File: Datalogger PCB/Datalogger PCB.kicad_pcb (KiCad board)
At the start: 2 copper layers, 42.2 x 101.8 mm, 46 parts, among them J1 Conn_01x02_Pin, M1 Motor_Servo, M2 Motor_Servo, M3 Motor_Servo, M4 Motor_Servo, U1 Teensy4.1, U2 BNO055, U3 LPS25HB, U4 AMS1117-5.0, U5 NRF24L01_Breakout, U6 VN5E160STR-E, U7 VN5E160STR-E, U8 VN5E160STR-E, U9 VN5E160STR-E

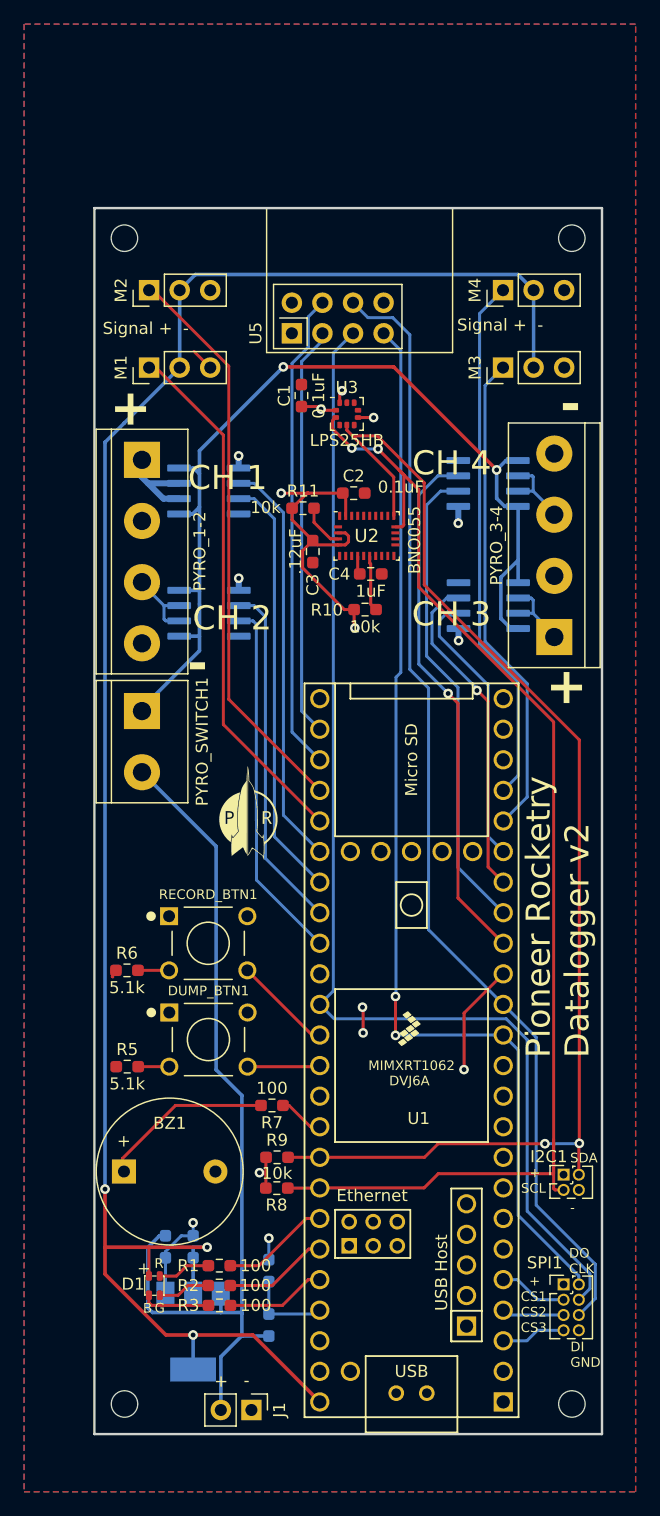
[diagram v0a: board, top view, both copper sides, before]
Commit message: Added serial connector and power connectors
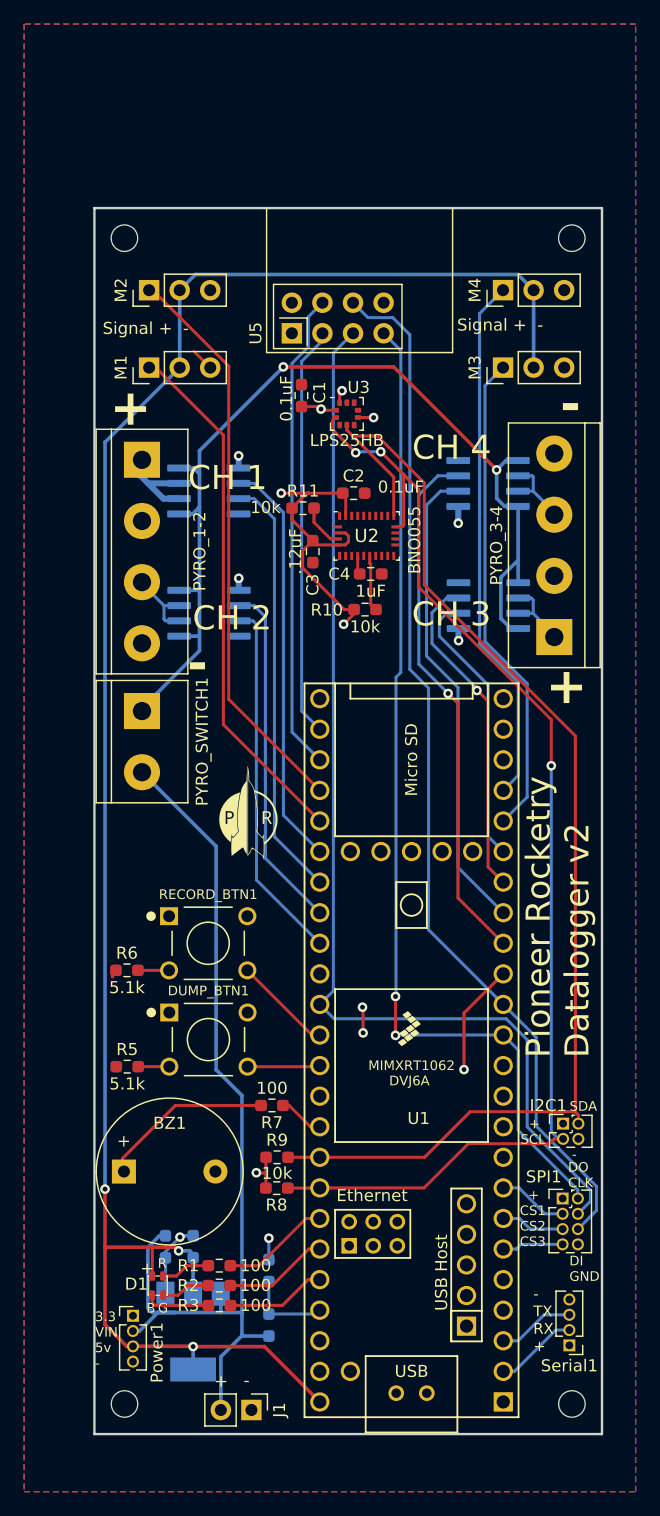
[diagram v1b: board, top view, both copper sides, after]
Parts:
- added Power1: Conn_01x04_Pin, Connector_PinHeader_1.27mm:PinHeader_1x04_P1.27mm_Vertical, F.Cu at (140.8, 134.2)
- added Serial1: Conn_01x04_Pin, Connector_PinHeader_1.27mm:PinHeader_1x04_P1.27mm_Vertical, F.Cu at (177.0, 136.7)
- moved SPI1 7.14 mm to (176.4, 124.5)
- moved I2C1 4.24 mm to (176.5, 118.2)
- moved D1 0.27 mm to (143.2, 132.5)
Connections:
- U1 pad 2: unconnected-(U1-0_RX1_CRX2_CS1-Pad2) -> /RX
- U1 pad 3: /EXTERNAL_CS3 -> /TX
- U1 pad 4: /EXTERNAL_CS2 -> unconnected-(U1-2_OUT2-Pad4)
- U1 pad 5: /EXTERNAL_CS1 -> unconnected-(U1-3_LRCLK2-Pad5)
- U1 pad 6: unconnected-(U1-4_BCLK2-Pad6) -> /EXTERNAL_CS3
- U1 pad 7: unconnected-(U1-5_IN2-Pad7) -> /EXTERNAL_CS2
- U1 pad 8: unconnected-(U1-6_OUT1D-Pad8) -> /EXTERNAL_CS1
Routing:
- net /DO: track 91.4 -> 84.2 mm
- net /CLK: track 99.5 -> 92.4 mm
- net /DI: track 94.2 -> 87.2 mm
- net /RX: track 0.00 -> 6.91 mm
- net /TX: track 0.00 -> 6.38 mm
- net /SCL: track 104.7 -> 99.6 mm, vias 2 -> 3
- net /VIN: track 76.4 -> 80.5 mm
- net /SDA: track 104.2 -> 100.7 mm, vias 2 -> 0
- net +5V: track 162.0 -> 160.8 mm
- net unconnected-(U1-2_OUT2-Pad4): track 0.00 -> 0.57 mm
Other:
- board text added: "- TX RX +"
- board text added: "3.3 VIN 5v -"

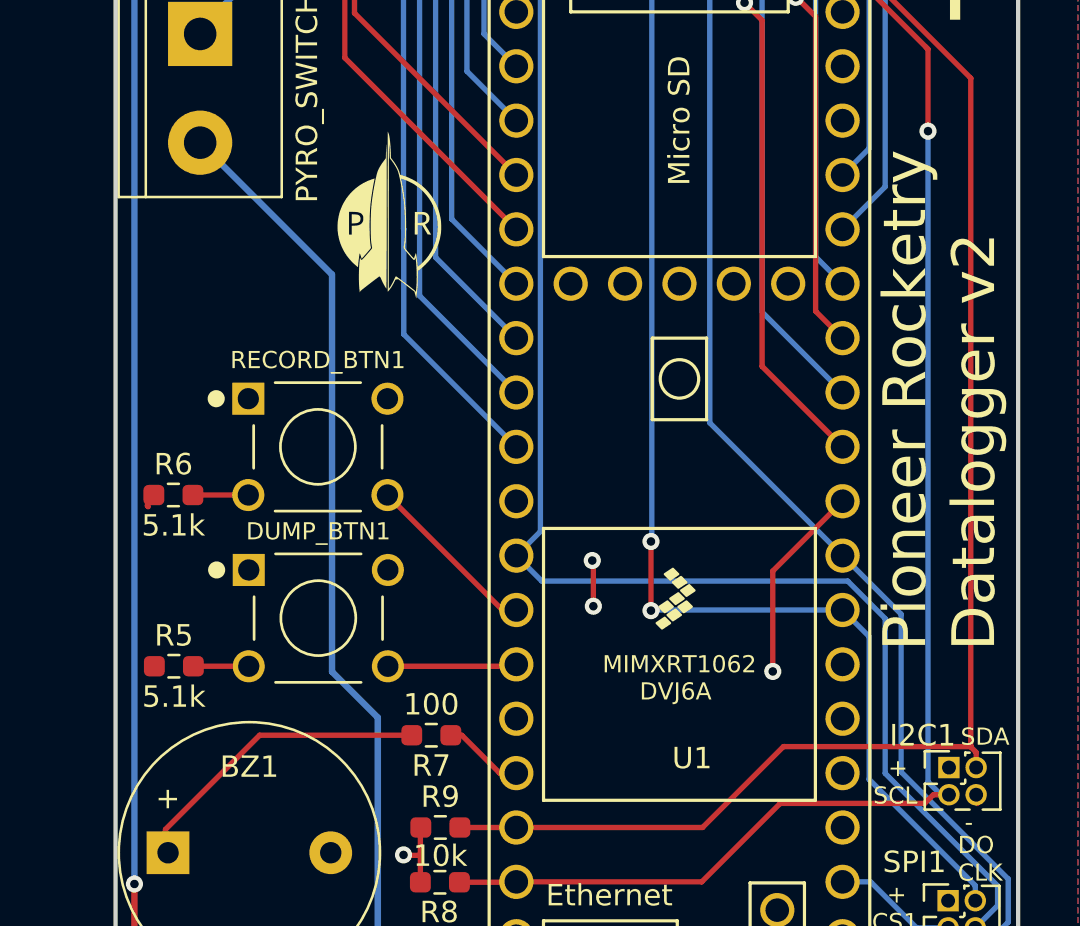
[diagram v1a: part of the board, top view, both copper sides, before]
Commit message: Remove DUMP_BTN
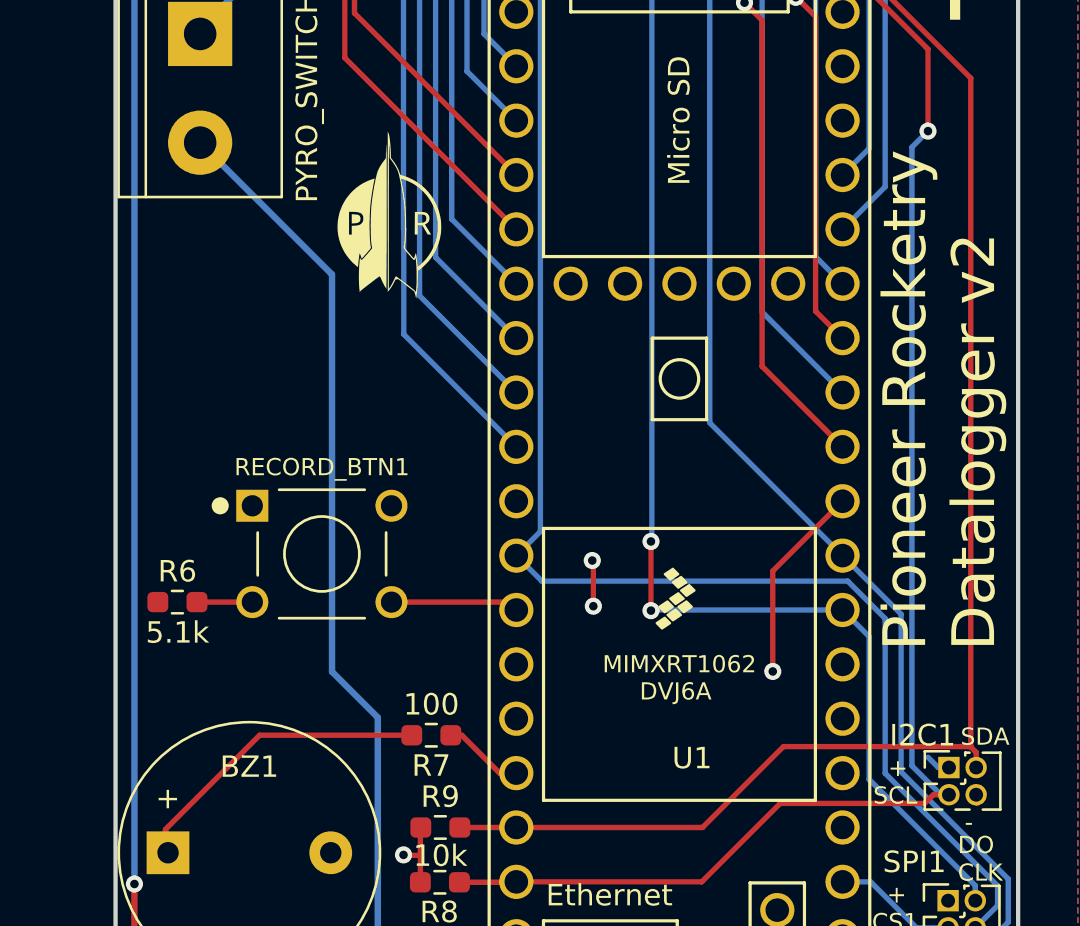
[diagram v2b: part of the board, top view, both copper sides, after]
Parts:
- removed DUMP_BTN1: FSM8JH, Push Button:SW_FSM8JH
- removed R5: 5.1k, Resistor_SMD:R_0603_1608Metric_Pad0.98x0.95mm_HandSolder
- moved R6 5.01 mm to (140.4, 110.5)
- moved RECORD_BTN1 5.01 mm to (147.2, 108.3)
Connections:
- U1 pad 37: /DUMP_BTN -> unconnected-(U1-15_A1_RX3_SPDIF_IN-Pad37)
- U1 pad 38: /ERASE_BTN -> unconnected-(U1-16_A2_RX4_SCL1-Pad38)
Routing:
- net /DUMP_BTN: track 6.04 -> 0.00 mm
- net Net-(DUMP_BTN1-Pad2): track 2.58 -> 0.00 mm
- net /RECORD_BTN: track 8.24 -> 6.63 mm
- net +3.3V: track 47.6 -> 48.8 mm
- net /SCL: track 99.6 -> 100.2 mm

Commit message: Final Revision
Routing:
- net +5V: track 160.8 -> 153.4 mm, vias 3 -> 0
- net /VIN: track 80.5 -> 74.7 mm, vias 0 -> 2
- net /PYRO_POWER: track 82.6 -> 87.4 mm, vias 2 -> 8
- added copper zone on In2.Cu, net +3.3V
- added copper zone on In1.Cu, net GND
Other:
- copper layers 2 -> 4

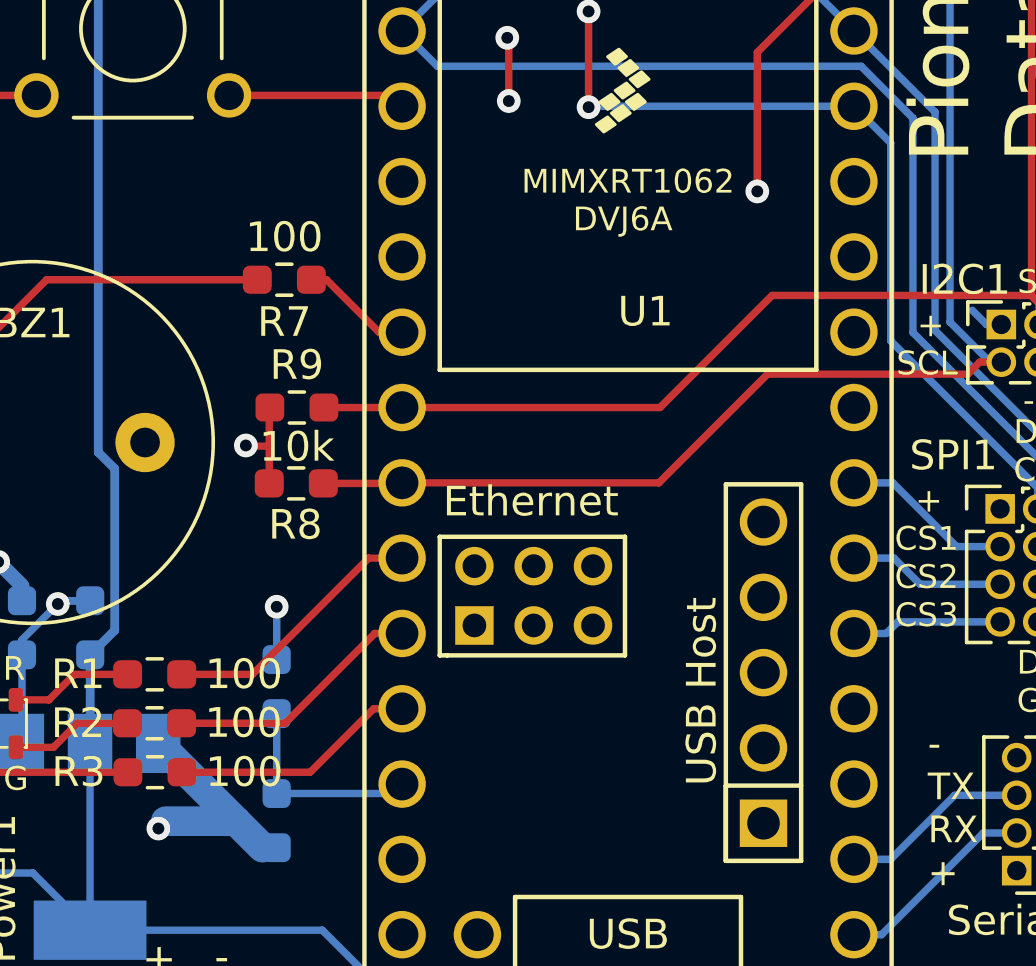
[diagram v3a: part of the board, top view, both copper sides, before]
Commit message: Made LED's connected to PWM pins
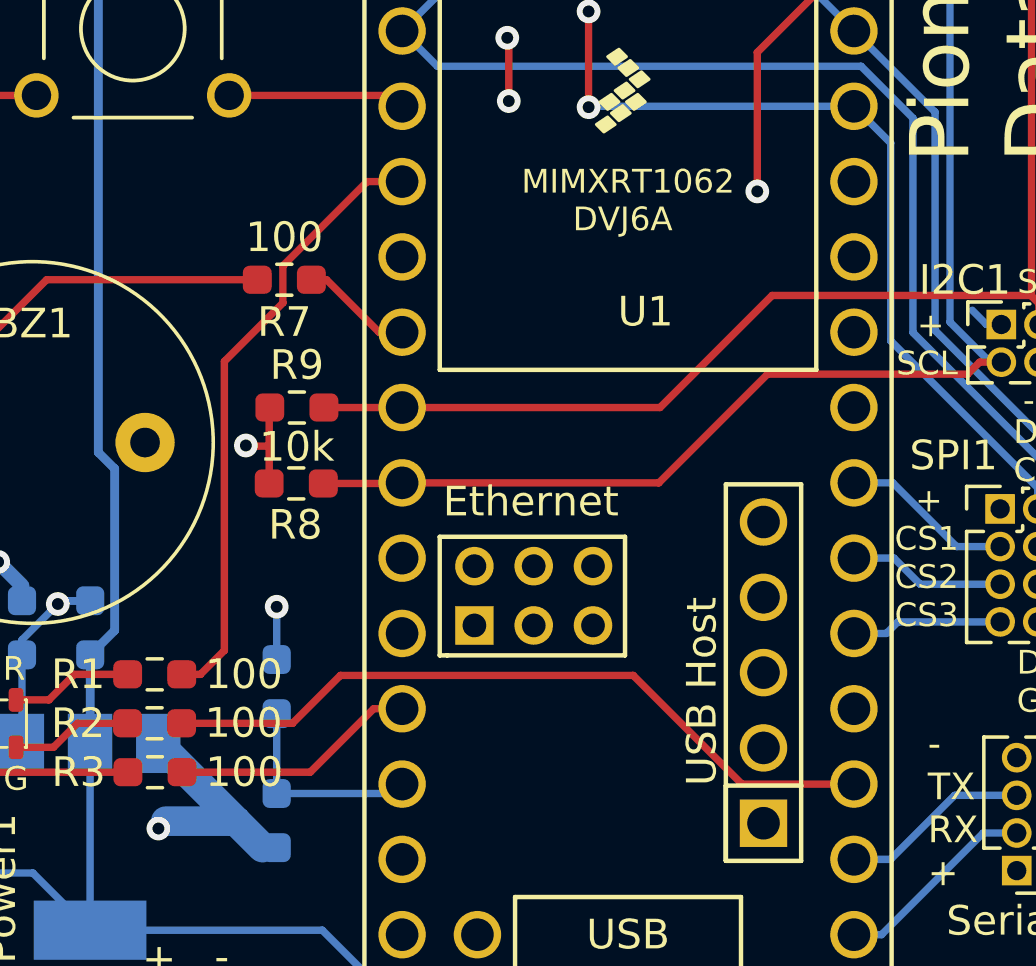
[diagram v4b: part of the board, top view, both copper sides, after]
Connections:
- U1 pad 37: unconnected-(U1-15_A1_RX3_SPDIF_IN-Pad37) -> /RGB-R
- U1 pad 4: unconnected-(U1-2_OUT2-Pad4) -> /RGB-G
- U1 pad 42: /RGB-R -> unconnected-(U1-20_A6_TX5_LRCLK1-Pad42)
- U1 pad 43: /RGB-G -> unconnected-(U1-21_A7_RX5_BCLK1-Pad43)
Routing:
- net /RGB-G: track 8.69 -> 25.4 mm
- net /RGB-R: track 9.06 -> 20.9 mm
- net unconnected-(U1-2_OUT2-Pad4): track 0.57 -> 0.00 mm
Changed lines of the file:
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@@
   (net 1 "GND")
   (net 2 "Net-(BZ1--)")
-  (net 3 "unconnected-(U1-15_A1_RX3_SPDIF_IN-Pad37)")
+  (net 3 "unconnected-(U1-20_A6_TX5_LRCLK1-Pad42)")
   (net 4 "unconnected-(U1-16_A2_RX4_SCL1-Pad38)")
   (net 5 "unconnected-(RECORD_BTN1-Pad3)")
@@
   (net 40 "/TX")
   (net 41 "/RX")
-  (net 42 "unconnected-(U1-2_OUT2-Pad4)")
+  (net 42 "unconnected-(U1-21_A7_RX5_BCLK1-Pad43)")
   (net 43 "unconnected-(U1-3_LRCLK2-Pad5)")
   (net 44 "unconnected-(U1-7_RX2_OUT1A-Pad9)")
@@
       (net 40 "/TX") (pinfunction "1_TX1_CTX2_MISO1") (pintype "bidirectional"))
     (pad "4" thru_hole circle (at -21.59 7.62 90) (size 1.6 1.6) (drill 1.1) (layers "*.Cu" "*.Mask")
-      (net 42 "unconnected-(U1-2_OUT2-Pad4)") (pinfunction "2_OUT2") (pintype "bidirectional+no_connect"))
+      (net 26 "/RGB-G") (pinfunction "2_OUT2") (pintype "bidirectional"))
     (pad "5" thru_hole circle (at -19.05 7.62 90) (size 1.6 1.6) (drill 1.1) (layers "*.Cu" "*.Mask")
       (net 43 "unconnected-(U1-3_LRCLK2-Pad5)") (pinfunction "3_LRCLK2") (pintype "bidirectional+no_connect"))
@@
       (net 29 "/RECORD_BTN") (pinfunction "14_A0_TX3_SPDIF_OUT") (pintype "bidirectional"))
     (pad "37" thru_hole circle (at -1.27 -7.62 90) (size 1.6 1.6) (drill 1.1) (layers "*.Cu" "*.Mask")
-      (net 3 "unconnected-(U1-15_A1_RX3_SPDIF_IN-Pad37)") (pinfunction "15_A1_RX3_SPDIF_IN") (pintype "bidirectional+no_connect"))
+      (net 25 "/RGB-R") (pinfunction "15_A1_RX3_SPDIF_IN") (pintype "bidirectional"))
     (pad "38" thru_hole circle (at -3.81 -7.62 90) (size 1.6 1.6) (drill 1.1) (layers "*.Cu" "*.Mask")
       (net 4 "unconnected-(U1-16_A2_RX4_SCL1-Pad38)") (pinfunction "16_A2_RX4_SCL1") (pintype "bidirectional+no_connect"))
@@
       (net 17 "/SCL") (pinfunction "19_A5_SCL") (pintype "bidirectional"))
     (pad "42" thru_hole circle (at -13.97 -7.62 90) (size 1.6 1.6) (drill 1.1) (layers "*.Cu" "*.Mask")
-      (net 25 "/RGB-R") (pinfunction "20_A6_TX5_LRCLK1") (pintype "bidirectional"))
+      (net 3 "unconnected-(U1-20_A6_TX5_LRCLK1-Pad42)") (pinfunction "20_A6_TX5_LRCLK1") (pintype "bidirectional"))
     (pad "43" thru_hole circle (at -16.51 -7.62 90) (size 1.6 1.6) (drill 1.1) (layers "*.Cu" "*.Mask")
-      (net 26 "/RGB-G") (pinfunction "21_A7_RX5_BCLK1") (pintype "bidirectional"))
+      (net 42 "unconnected-(U1-21_A7_RX5_BCLK1-Pad43)") (pinfunction "21_A7_RX5_BCLK1") (pintype "bidirectional"))
     (pad "44" thru_hole circle (at -19.05 -7.62 90) (size 1.6 1.6) (drill 1.1) (layers "*.Cu" "*.Mask")
       (net 27 "/RGB-B") (pinfunction "22_A8_CTX1") (pintype "bidirectional"))
@@
   (segment (start 151.385 116.72) (end 144.28 116.72) (width 0.25) (layer "F.Cu") (net 2))
   (segment (start 139.88 121.12) (end 139.88 122.21) (width 0.25) (layer "F.Cu") (net 2))
-  (segment (start 156.18 113.5) (end 156.27 113.41) (width 0.25) (layer "F.Cu") (net 3))
   (segment (start 141.35 110.5025) (end 143.9375 110.5025) (width 0.25) (layer "F.Cu") (net 6))
   (segment (start 158.1725 65.86) (end 158.4175 66.105) (width 0.25) (layer "F.Cu") (net 7))
@@
   (segment (start 166.2 77.74) (end 170.25 81.79) (width 0.25) (layer "B.Cu") (net 24))
   (segment (start 170.25 81.79) (end 170.25 94.37) (width 0.25) (layer "B.Cu") (net 24))
-  (segment (start 151.22 130.03) (end 155.14 126.11) (width 0.25) (layer "F.Cu") (net 25))
-  (segment (start 155.14 126.11) (end 156.27 126.11) (width 0.25) (layer "F.Cu") (net 25))
-  (segment (start 148.8375 130.03) (end 151.22 130.03) (width 0.25) (layer "F.Cu") (net 25))
-  (segment (start 152.32 131.68) (end 155.35 128.65) (width 0.25) (layer "F.Cu") (net 26))
-  (segment (start 155.35 128.65) (end 156.27 128.65) (width 0.25) (layer "F.Cu") (net 26))
-  (segment (start 148.8325 131.68) (end 152.32 131.68) (width 0.25) (layer "F.Cu") (net 26))
+  (segment (start 152.25 117.5) (end 152.25 116.25) (width 0.25) (layer "F.Cu") (net 25))
+  (segment (start 156.18 113.5) (end 156.27 113.41) (width 0.25) (layer "F.Cu") (net 25))
+  (segment (start 149.47 130.03) (end 150.275 129.225) (width 0.25) (layer "F.Cu") (net 25))
+  (segment (start 152.25 116.25) (end 155.09 113.41) (width 0.25) (layer "F.Cu") (net 25))
+  (segment (start 148.8375 130.03) (end 149.47 130.03) (width 0.25) (layer "F.Cu") (net 25))
+  (segment (start 150.275 129.225) (end 150.275 119.475) (width 0.25) (layer "F.Cu") (net 25))
+  (segment (start 155.09 113.41) (end 156.27 113.41) (width 0.25) (layer "F.Cu") (net 25))
+  (segment (start 150.275 119.475) (end 152.25 117.5) (width 0.25) (layer "F.Cu") (net 25))
+  (segment (start 148.8325 131.68) (end 152.57625 131.68) (width 0.25) (layer "F.Cu") (net 26))
+  (segment (start 154.19125 130.065) (end 164.065 130.065) (width 0.25) (layer "F.Cu") (net 26))
+  (segment (start 152.57625 131.68) (end 154.19125 130.065) (width 0.25) (layer "F.Cu") (net 26))
+  (segment (start 167.73 133.73) (end 171.51 133.73) (width 0.25) (layer "F.Cu") (net 26))
+  (segment (start 164.065 130.065) (end 167.73 133.73) (width 0.25) (layer "F.Cu") (net 26))
+  (segment (start 171.51 133.73) (end 171.91 134.13) (width 0.25) (layer "B.Cu") (net 26))
   (segment (start 153.17 133.33) (end 155.31 131.19) (width 0.25) (layer "F.Cu") (net 27))
   (segment (start 148.8475 133.33) (end 153.17 133.33) (width 0.25) (layer "F.Cu") (net 27))
@@
   (segment (start 175.87 135.38) (end 177 135.38) (width 0.25) (layer "B.Cu") (net 41))
   (segment (start 171.51 138.81) (end 172.44 138.81) (width 0.25) (layer "B.Cu") (net 41))
-  (segment (start 171.51 133.73) (end 171.91 134.13) (width 0.25) (layer "B.Cu") (net 42))
   (segment (start 141.366904 64.404904) (end 141.366904 63.075) (width 1.25) (layer "B.Cu") (net 88))
   (segment (start 142.0114 65.0494) (end 141.366904 64.404904) (width 1.25) (layer "B.Cu") (net 88))
